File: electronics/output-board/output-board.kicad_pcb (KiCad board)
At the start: 2 copper layers, 105.2 x 77.5 mm, 91 parts, among them J1 Conn_01x02_Male, J10 Conn_01x02_Male, J11 Conn_01x02_Male, J12 Conn_01x02_Male, J13 Conn_01x02_Male, J14 Arming switch, J15 Conn_01x02_Male, J16 Conn_01x02_Male, J17 Conn_01x02_Male, J18 Conn_01x02_Male, J19 Extra IO, J2 Conn_01x02_Male, J3 12V In, J4 Conn_01x02, J5 SWD Header, J6 Conn_01x02, J7 Conn_01x02_Male, J8 Conn_01x02_Male, J9 Conn_01x02_Male, SW1 SW_Push_Dual, U1 MAX33012EASA+, U2 LD3985M33R_SOT23, U3 STM32F105VBH6

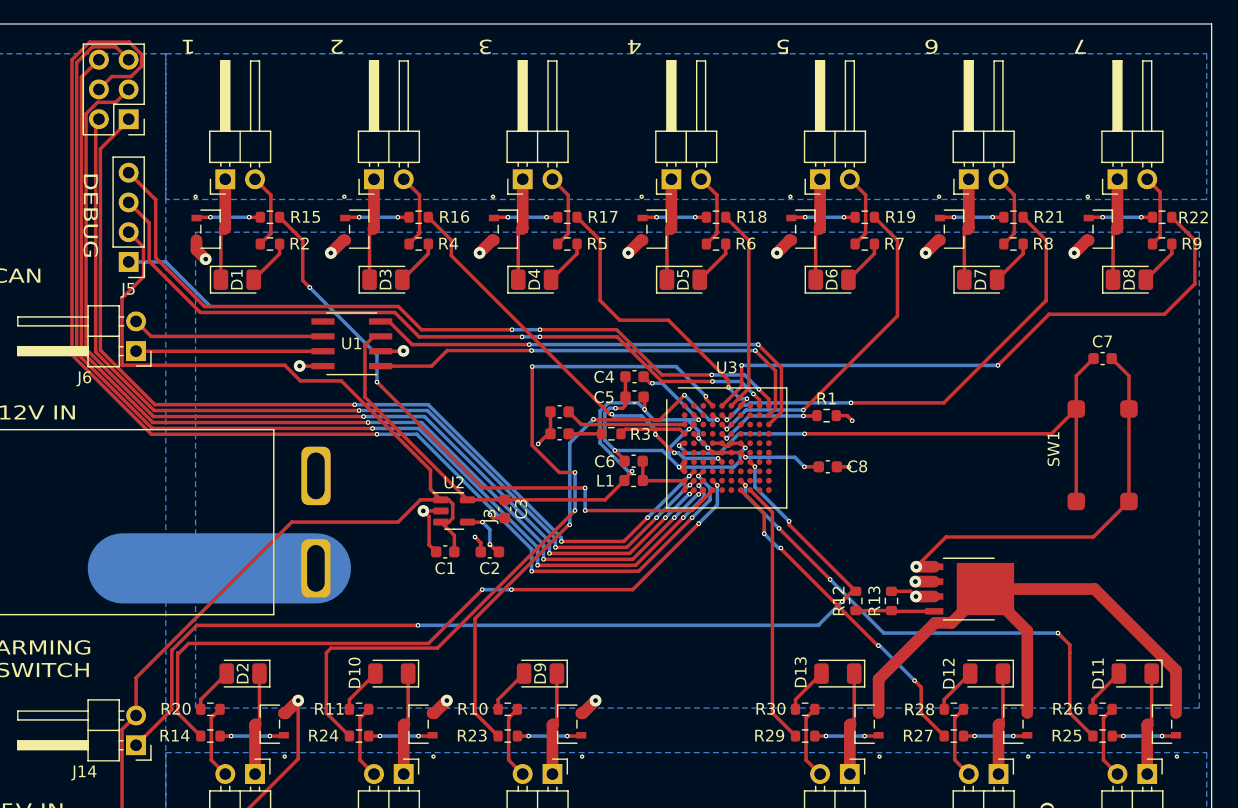
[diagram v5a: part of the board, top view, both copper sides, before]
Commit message: continued working on four-layer output board
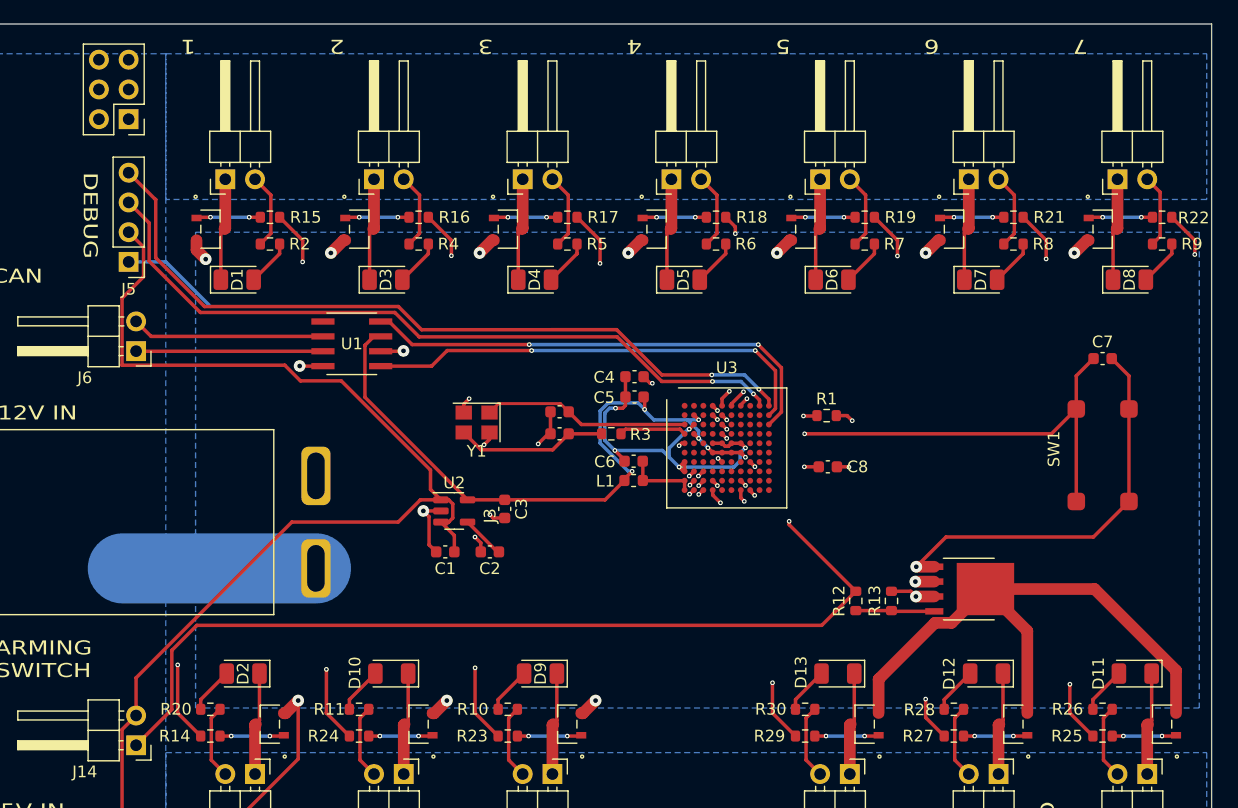
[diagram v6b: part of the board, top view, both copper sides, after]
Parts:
- added Y1: 25MHz 9pF, Crystal:Crystal_SMD_3225-4Pin_3.2x2.5mm, F.Cu at (105.3, 130.6)
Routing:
- net /MOSFET-sheet9/INPUT: track 65.7 -> 50.4 mm, vias 4 -> 2
- net Net-(C11-Pad2): track 2.82 -> 13.0 mm
- net Net-(C10-Pad2): track 10.4 -> 17.7 mm
- net /MOSFET-sheet8/INPUT: track 45.0 -> 38.7 mm, vias 4 -> 2
- net /MOSFET-sheet5/INPUT: track 28.4 -> 25.5 mm
- net GND: track 138.4 -> 141.0 mm, vias 26 -> 28
- net /MOSFET-sheet10/INPUT: track 43.0 -> 40.6 mm, vias 4 -> 2
- net /MOSFET-sheet7/INPUT: track 52.2 -> 50.1 mm
- net /MOSFET-sheet3/INPUT: track 25.1 -> 23.6 mm
- net Net-(J19-Pad4): track 106.5 -> 105.2 mm, vias 4 -> 1
- net /MOSFET-sheet6/INPUT: track 40.0 -> 41.3 mm
- net /MOSFET-sheet/INPUT: track 61.5 -> 60.5 mm, vias 4 -> 2
- net Net-(J19-Pad5): track 96.4 -> 95.5 mm, vias 4 -> 1
- net Net-(J19-Pad6): track 89.2 -> 88.4 mm, vias 4 -> 1
- net Net-(C2-Pad1): track 4.48 -> 3.87 mm, vias 2 -> 0
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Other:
- copper layers 2 -> 4

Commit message: finished (mostly) output board
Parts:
- added C12: 100nF, Capacitor_SMD:C_0603_1608Metric, F.Cu at (137.0, 136.0)
- added C13: 100nF, Capacitor_SMD:C_0603_1608Metric, F.Cu at (137.0, 138.0)
- added C9: 100nF, Capacitor_SMD:C_0603_1608Metric, F.Cu at (137.0, 140.0)
- R13: value 100K -> 10K
- moved C5 10.3 mm to (115.0, 138.0)
- moved C4 10.1 mm to (115.0, 136.0)
- moved L1 8.35 mm to (115.0, 143.0)
- moved C6 7.17 mm to (115.0, 140.0)
- moved C8 1.75 mm to (137.0, 134.0)
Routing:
- net +3V3: track 71.2 -> 131.8 mm, vias 8 -> 12
- net GND: track 141.0 -> 126.6 mm, vias 28 -> 32
- net VDDA: track 6.03 -> 12.9 mm
- net /MOSFET-sheet8/INPUT: track 38.7 -> 41.0 mm
- net Net-(C7-Pad1): track 49.1 -> 48.0 mm
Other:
- board text added: "RESET"

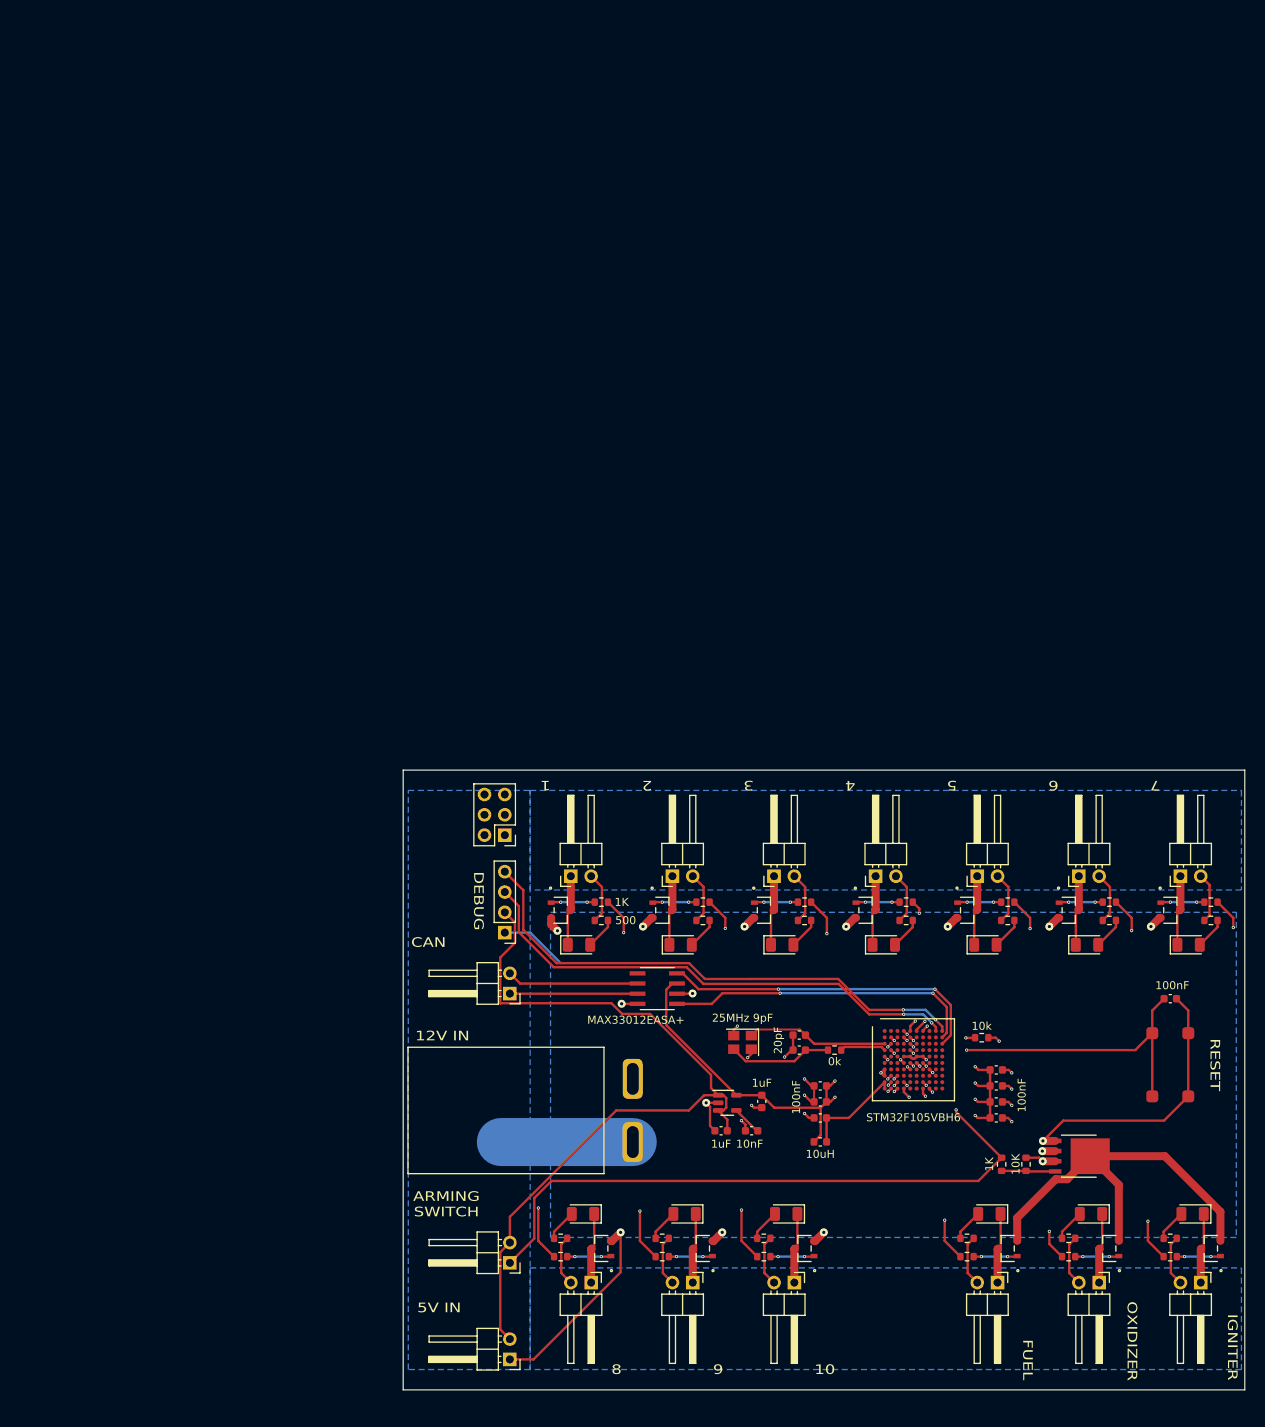
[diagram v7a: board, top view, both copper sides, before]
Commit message: Minor routing changes
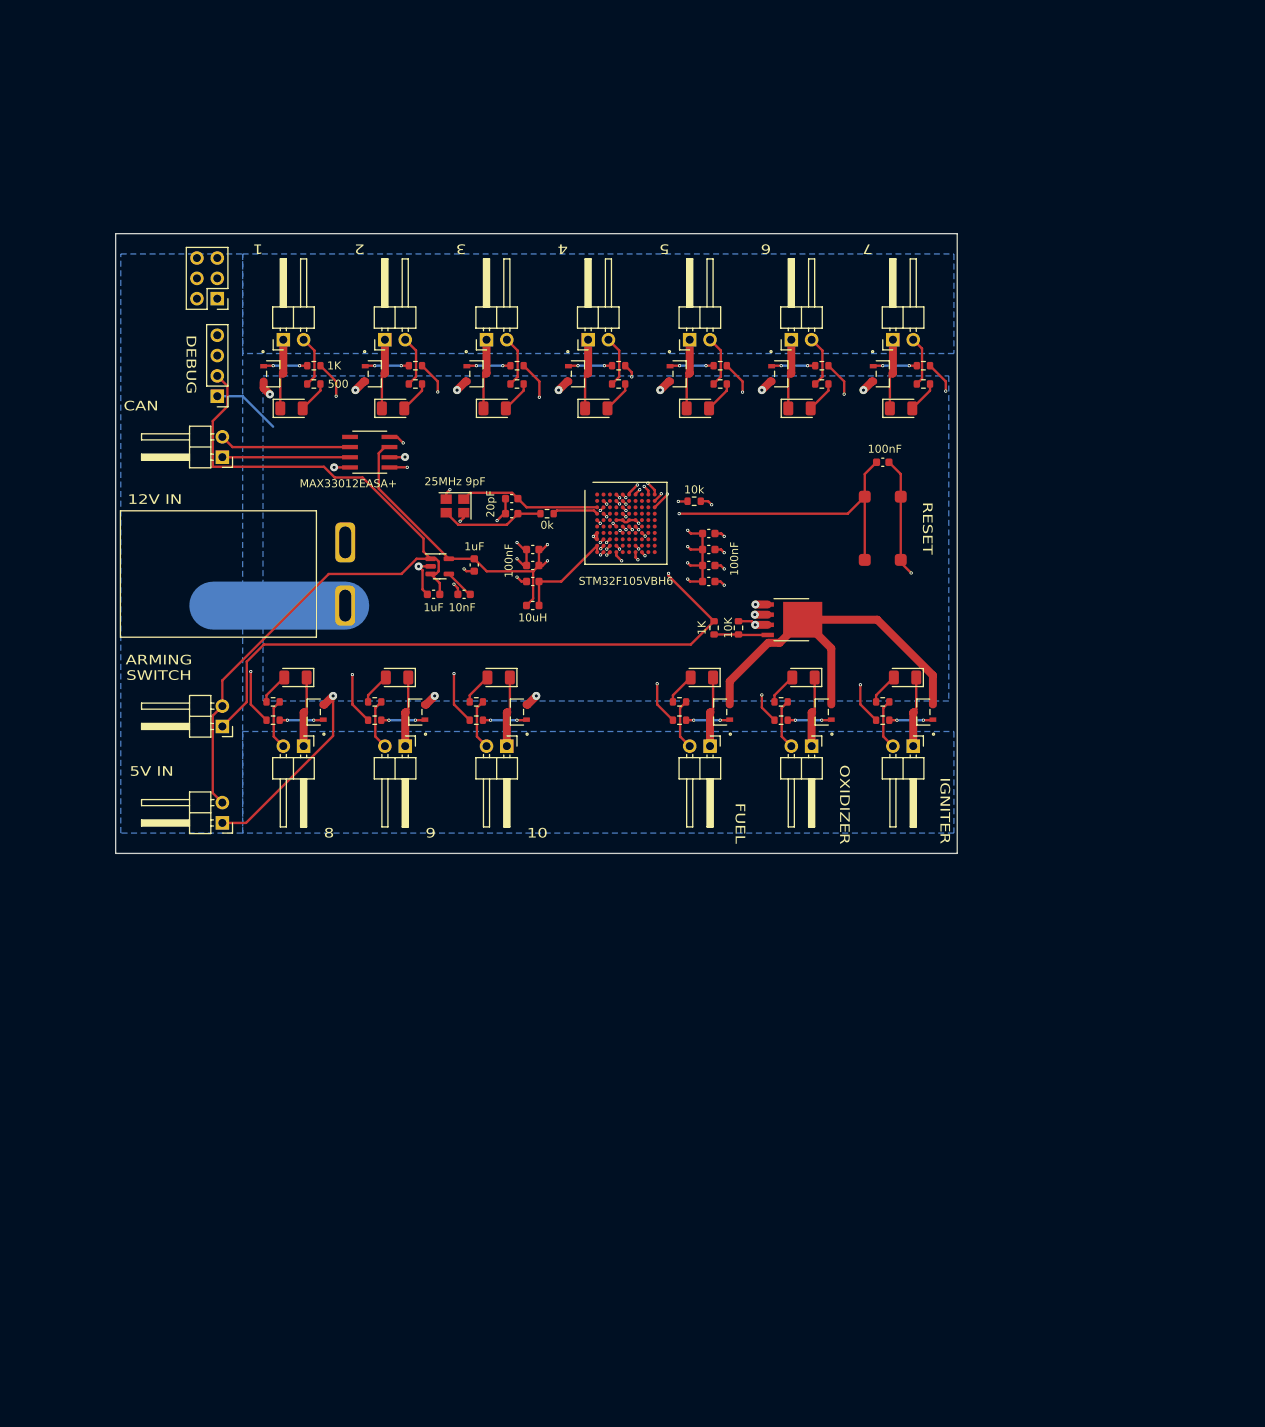
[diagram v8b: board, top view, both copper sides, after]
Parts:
- moved C10 76.1 mm to (76.4, 62.6)
- moved D10 76.1 mm to (62.1, 84.9)
- moved D12 76.1 mm to (112.9, 84.9)
- moved D13 76.1 mm to (100.2, 84.9)
- moved D2 76.1 mm to (49.4, 84.9)
- moved D9 76.1 mm to (74.8, 84.9)
- moved J1 76.1 mm to (47.9, 42.7)
- moved J11 76.1 mm to (124.1, 42.7)
- moved J12 76.1 mm to (75.8, 93.5)
- moved J13 76.1 mm to (63.1, 93.5)
- moved J14 76.1 mm to (40.3, 91.1)
- moved J15 76.1 mm to (126.6, 93.5)
- moved J16 76.1 mm to (113.9, 93.5)
- moved J17 76.1 mm to (101.2, 93.5)
- moved J18 76.1 mm to (50.4, 93.5)
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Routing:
- net GND: track 126.6 -> 108.3 mm, vias 32 -> 33
- net /CAN_TX: track 39.0 -> 36.7 mm
- net /CAN_RX: track 41.2 -> 40.3 mm
- net /SWCLK: track 63.3 -> 63.5 mm, vias 2 -> 1
- net /SWDIO: track 66.2 -> 66.0 mm, vias 2 -> 1
